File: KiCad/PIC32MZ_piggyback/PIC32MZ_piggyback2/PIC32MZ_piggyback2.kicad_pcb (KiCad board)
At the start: 2 copper layers, 12 parts, among them J1 Conn_02x13_Odd_Even, J1-1 Conn_01x13_Male, J1-2 Conn_01x13_Male, J2 Conn_02x13_Odd_Even, J2-1 Conn_01x13_Male, J2-2 Conn_01x13_Male, J3 Conn_02x13_Odd_Even, J3-1 Conn_01x13_Male, J3-2 Conn_01x13_Male, J4 Conn_02x13_Odd_Even, J4-1 Conn_01x13_Male, J4-2 Conn_01x13_Male

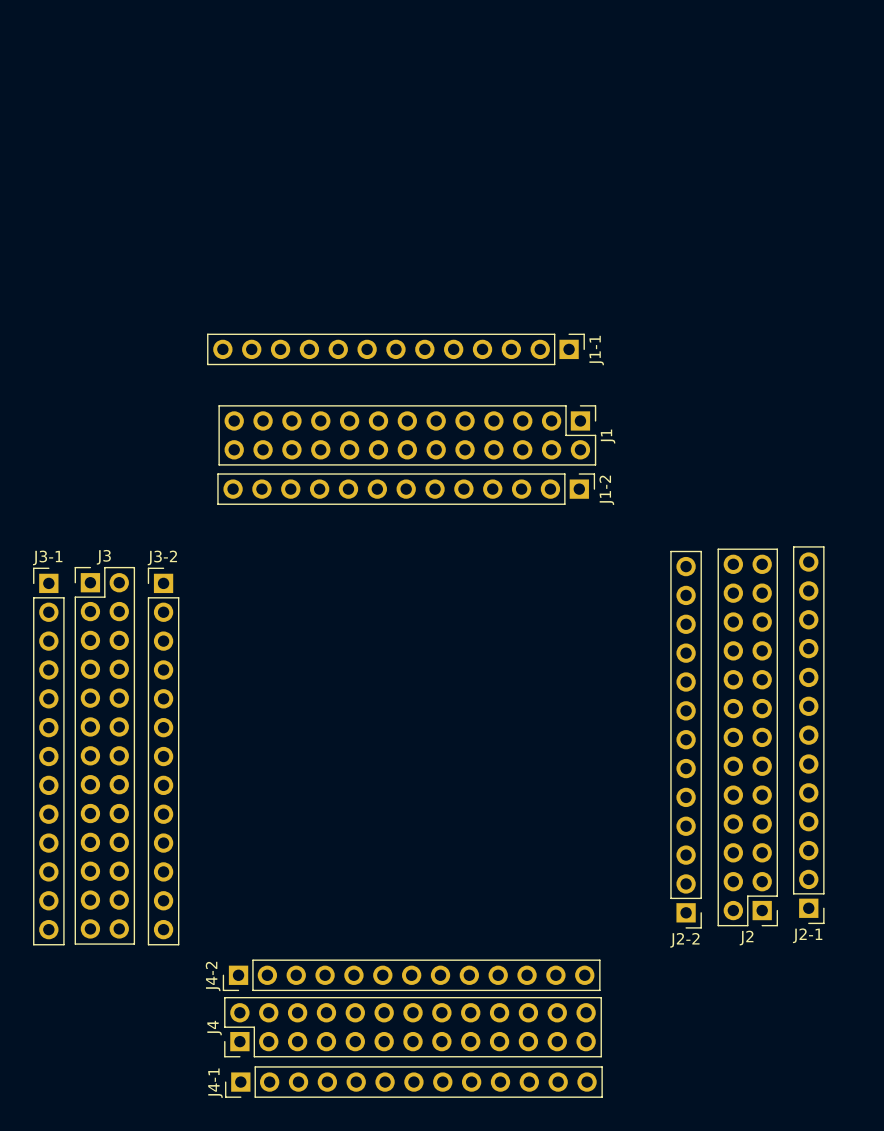
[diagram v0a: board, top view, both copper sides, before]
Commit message: pre-finish of the drawings. To be checked.
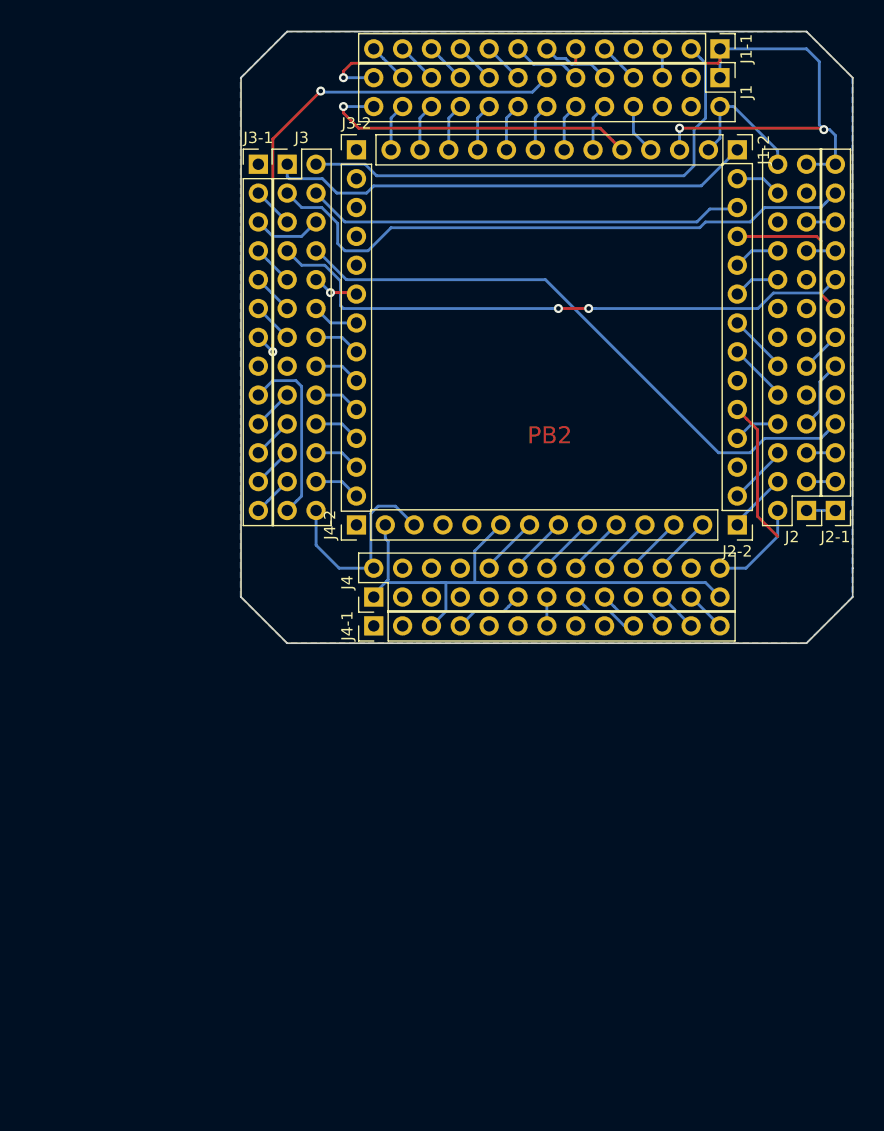
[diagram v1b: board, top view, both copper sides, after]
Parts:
- moved J4-1 41.8 mm to (133.6, 91.4)
- moved J3-2 41.8 mm to (132.1, 49.5)
- moved J3-1 41.3 mm to (123.4, 50.8)
- moved J4-2 41.0 mm to (132.1, 82.5)
- moved J4 40.9 mm to (133.6, 88.9)
- moved J3 40.7 mm to (126.0, 50.8)
- moved J2 35.4 mm to (171.7, 81.3)
- moved J2-1 35.1 mm to (174.2, 81.3)
- moved J2-2 34.4 mm to (165.6, 82.5)
- moved J1-2 32.9 mm to (165.6, 49.5)
- moved J1 32.6 mm to (164.1, 43.2)
- moved J1-1 29.6 mm to (164.1, 40.6)
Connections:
- J1 pad 3: /RE5 -> (no net)
- J1 pad 4: /RG15 -> (no net)
- J1 pad 6: /RE6 -> (no net)
- J1-1 pad 10: Net-(J1-1-Pad10) -> /RE9
- J1-1 pad 11: Net-(J1-1-Pad11) -> /RB4
- J1-1 pad 12: Net-(J1-1-Pad12) -> /RB2
- J1-1 pad 13: Net-(J1-1-Pad13) -> /RB0
- J1-1 pad 2: Net-(J1-1-Pad2) -> /TXP
- J1-1 pad 3: Net-(J1-1-Pad3) -> /RE7
- J1-1 pad 5: Net-(J1-1-Pad5) -> /RC2
- J1-1 pad 7: Net-(J1-1-Pad7) -> /RC4
- J1-1 pad 8: Net-(J1-1-Pad8) -> /RG7
- J1-1 pad 9: Net-(J1-1-Pad9) -> /RA0
- J1-2 pad 1: Net-(J1-2-Pad1) -> /TXN
- J1-2 pad 10: Net-(J1-2-Pad10) -> /RE8
- J1-2 pad 11: Net-(J1-2-Pad11) -> /RB5
- J1-2 pad 12: Net-(J1-2-Pad12) -> /RB3
- J1-2 pad 13: Net-(J1-2-Pad13) -> /RB1
- J1-2 pad 4: Net-(J1-2-Pad4) -> /RC1
- J1-2 pad 6: Net-(J1-2-Pad6) -> /RC3
- J1-2 pad 7: Net-(J1-2-Pad7) -> /RG6
- J1-2 pad 8: Net-(J1-2-Pad8) -> /RG8
- J1-2 pad 9: Net-(J1-2-Pad9) -> /RG9
- J2 pad 13: /RG0 -> (no net)
- J2 pad 14: /RG1 -> (no net)
- J2 pad 15: /RA7 -> (no net)
- J2 pad 16: /RA6 -> (no net)
- J2 pad 17: /RE1 -> (no net)
- J2 pad 22: /RG13 -> (no net)
- J2 pad 23: /RE4 -> (no net)
- J2 pad 9: Net-(J2-Pad9) -> (no net)
- J2-1 pad 1: Net-(J2-1-Pad1) -> /RD1
- J2-1 pad 10: Net-(J2-1-Pad10) -> /RG12
- J2-1 pad 11: Net-(J2-1-Pad11) -> /RE2
- J2-1 pad 12: Net-(J2-1-Pad12) -> /RXN
- J2-1 pad 2: Net-(J2-1-Pad2) -> /RD3
- J2-1 pad 3: Net-(J2-1-Pad3) -> /RD12
- J2-1 pad 6: Net-(J2-1-Pad6) -> /RD4
- J2-1 pad 7: Net-(J2-1-Pad7) -> /RF1
- J2-2 pad 1: Net-(J2-2-Pad1) -> /RD2
- J2-2 pad 10: Net-(J2-2-Pad10) -> /RG14
- J2-2 pad 12: Net-(J2-2-Pad12) -> /RXP
- J2-2 pad 13: Net-(J2-2-Pad13) -> /RE3
- J2-2 pad 2: Net-(J2-2-Pad2) -> /RD13
- J2-2 pad 3: Net-(J2-2-Pad3) -> (no net)
- J2-2 pad 4: Net-(J2-2-Pad4) -> /RD5
- J2-2 pad 7: Net-(J2-2-Pad7) -> /RD7
- J2-2 pad 8: Net-(J2-2-Pad8) -> /RF0
- J2-2 pad 9: Net-(J2-2-Pad9) -> /RE0
- J3 pad 15: /RF13 -> (no net)
- J3-1 pad 1: Net-(J3-1-Pad1) -> (no net)
- J3-1 pad 10: Net-(J3-1-Pad10) -> /RB12
- J3-1 pad 11: Net-(J3-1-Pad11) -> /RB14
- J3-1 pad 12: Net-(J3-1-Pad12) -> /RD14
- J3-1 pad 13: Net-(J3-1-Pad13) -> /RF4
- J3-1 pad 2: Net-(J3-1-Pad2) -> /LED1
- J3-1 pad 3: Net-(J3-1-Pad3) -> /LED2
- J3-1 pad 4: Net-(J3-1-Pad4) -> /RA9
- J3-1 pad 5: Net-(J3-1-Pad5) -> /RB8
- J3-1 pad 6: Net-(J3-1-Pad6) -> /RB10
- J3-2 pad 1: Net-(J3-2-Pad1) -> (no net)
- J3-2 pad 10: Net-(J3-2-Pad10) -> /RF12
- J3-2 pad 11: Net-(J3-2-Pad11) -> /RB13
- J3-2 pad 12: Net-(J3-2-Pad12) -> /RB15
- J3-2 pad 13: Net-(J3-2-Pad13) -> /RF5
- J3-2 pad 2: Net-(J3-2-Pad2) -> (no net)
- J3-2 pad 3: Net-(J3-2-Pad3) -> (no net)
- J3-2 pad 4: Net-(J3-2-Pad4) -> (no net)
- J3-2 pad 5: Net-(J3-2-Pad5) -> (no net)
- J3-2 pad 6: Net-(J3-2-Pad6) -> /RA10
- J3-2 pad 7: Net-(J3-2-Pad7) -> /RB9
- J3-2 pad 8: Net-(J3-2-Pad8) -> /RB11
- J3-2 pad 9: Net-(J3-2-Pad9) -> /RA1
- J4 pad 19: Net-(J4-Pad19) -> (no net)
- J4 pad 24: Net-(J4-Pad24) -> (no net)
- J4 pad 3: Net-(J4-Pad3) -> (no net)
- J4 pad 4: Net-(J4-Pad4) -> (no net)
- J4 pad 5: /USB-D_P -> (no net)
- J4 pad 6: /USB-D_N -> (no net)
- J4 pad 7: /USB-VBUS -> (no net)
- J4 pad 8: Net-(J4-Pad8) -> (no net)
- J4 pad 9: Net-(J4-Pad9) -> (no net)
- J4-1 pad 1: Net-(J4-1-Pad1) -> (no net)
- J4-1 pad 10: Net-(J4-1-Pad10) -> /RA4
- J4-1 pad 11: Net-(J4-1-Pad11) -> /RA14
- J4-1 pad 12: Net-(J4-1-Pad12) -> /RD10
- J4-1 pad 13: Net-(J4-1-Pad13) -> /RD0
- J4-1 pad 2: Net-(J4-1-Pad2) -> (no net)
- J4-1 pad 4: Net-(J4-1-Pad4) -> /MCU_MISO
- J4-1 pad 5: Net-(J4-1-Pad5) -> /LED1
- J4-1 pad 7: Net-(J4-1-Pad7) -> /RA2
- J4-1 pad 9: Net-(J4-1-Pad9) -> (no net)
- J4-2 pad 1: Net-(J4-2-Pad1) -> (no net)
- J4-2 pad 10: Net-(J4-2-Pad10) -> /RA3
- J4-2 pad 11: Net-(J4-2-Pad11) -> /RA5
- J4-2 pad 12: Net-(J4-2-Pad12) -> /RA15
- J4-2 pad 13: Net-(J4-2-Pad13) -> /RD9
- J4-2 pad 4: Net-(J4-2-Pad4) -> (no net)
- J4-2 pad 5: Net-(J4-2-Pad5) -> /LED2
- J4-2 pad 7: Net-(J4-2-Pad7) -> /RF3
- J4-2 pad 8: Net-(J4-2-Pad8) -> /MCU_SCK
- J4-2 pad 9: Net-(J4-2-Pad9) -> /MCU_MOSI
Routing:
- net /VCC: track 0.00 -> 141.9 mm, vias 0 -> 3
- net /GND: track 0.00 -> 95.1 mm, vias 0 -> 1
- net /RB7: track 0.00 -> 54.1 mm
- net /RXN: track 0.00 -> 53.5 mm
- net /RB6: track 0.00 -> 52.7 mm, vias 0 -> 2
- net /MCLR: track 0.00 -> 47.0 mm, vias 0 -> 2
- net /TXP: track 0.00 -> 45.3 mm
- net /TXN: track 0.00 -> 42.9 mm
- net /RXP: track 0.00 -> 38.7 mm
- net /RC4: track 0.00 -> 6.13 mm
- net /RA4: track 0.00 -> 6.13 mm
- net /MCU_MISO: track 0.00 -> 6.13 mm
- net /RD4: track 0.00 -> 6.13 mm
- net /LED2: track 0.00 -> 6.13 mm
- net /RA14: track 0.00 -> 6.13 mm
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- added copper zone on B.Cu, net /GND
- added copper zone on F.Cu, net /GND
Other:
- board outline added: 53.8 x 53.8 mm
- board text added: "PB2"
